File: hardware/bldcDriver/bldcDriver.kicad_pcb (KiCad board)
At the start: 2 copper layers, 5 parts, among them Q1 NMOS, U2 STM32G431RBTx

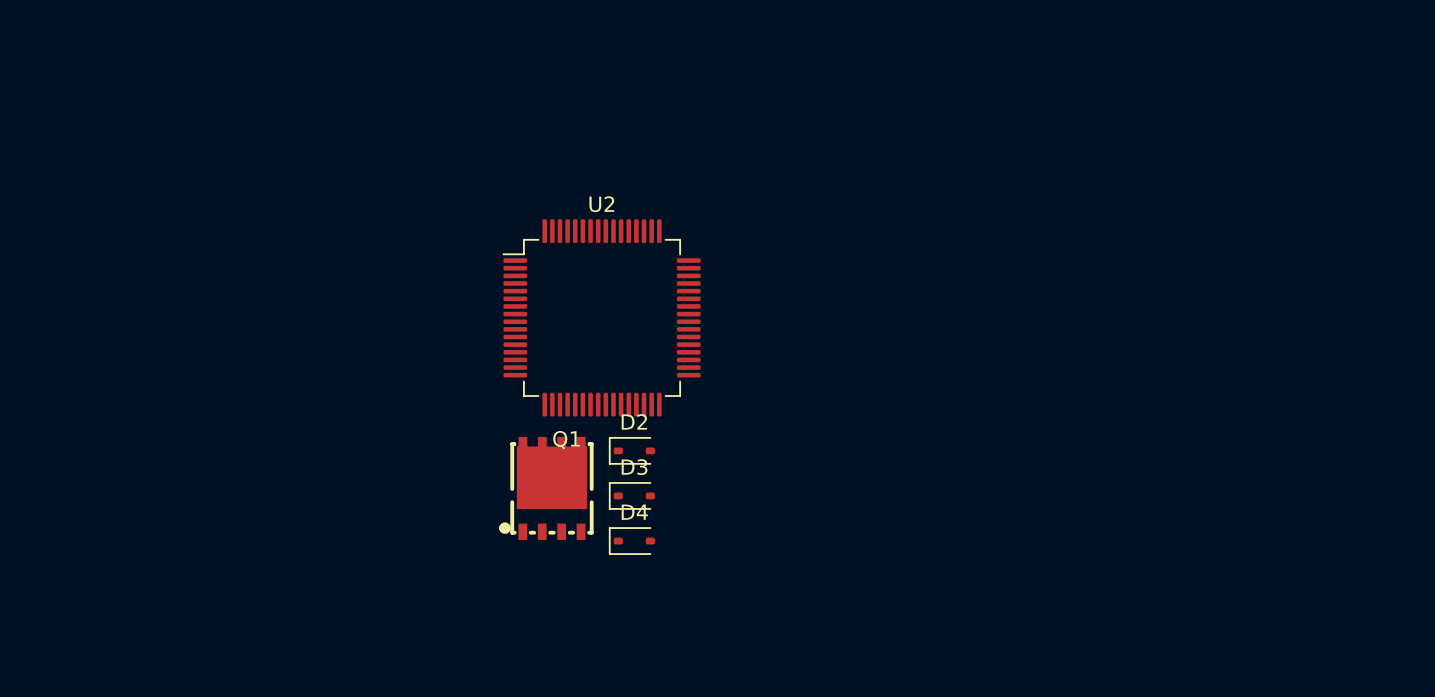
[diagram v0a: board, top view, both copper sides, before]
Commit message: motorDriver sch update
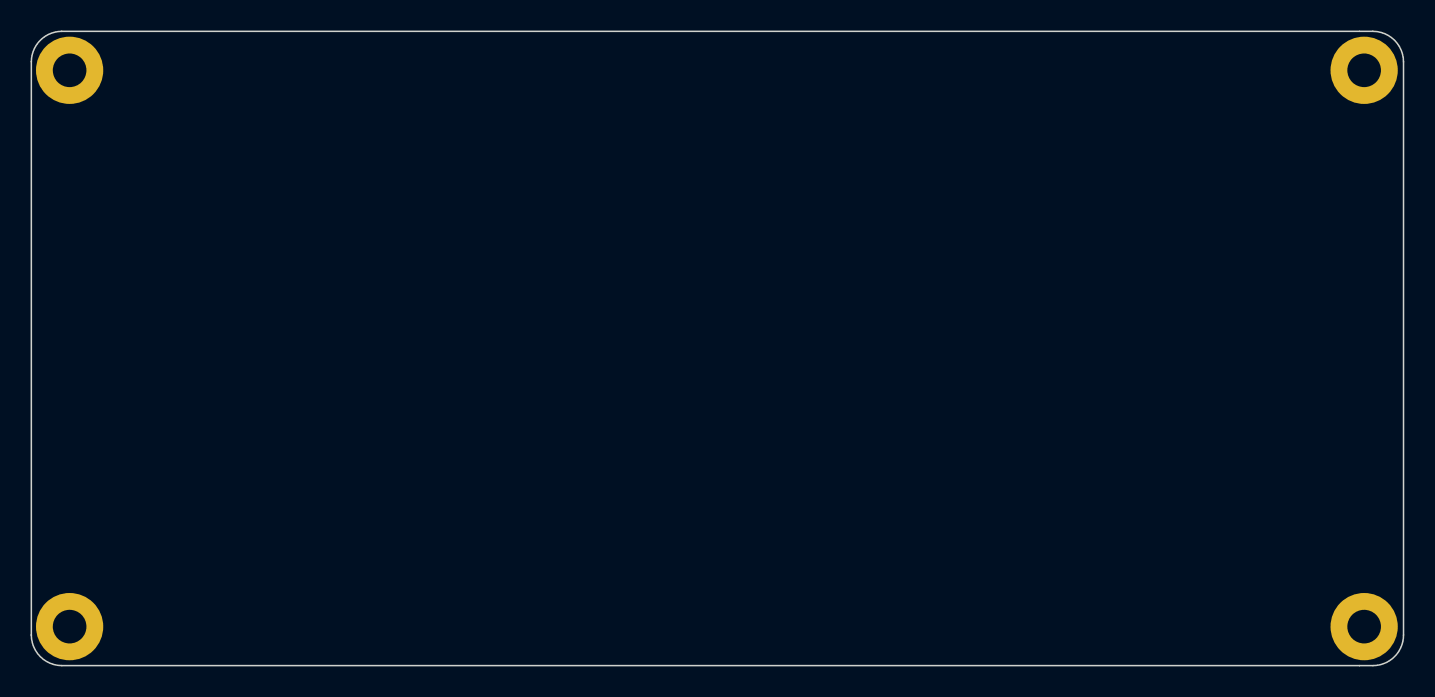
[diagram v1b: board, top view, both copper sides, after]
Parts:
- removed D2, D3, D4: 1N5819WS, Diode_SMD:D_SOD-323
- removed Q1: NMOS, balancerDriver:PDFN-8_L4.9-W5.8-P1.27-LS6.1-BL
- removed U2: STM32G431RBTx, Package_QFP:LQFP-64_10x10mm_P0.5mm
- added ?: , , F.Cu at (56.0, 57.6)
- added ?: , , F.Cu at (140.7, 57.6)
- added ?: , , F.Cu at (140.7, 94.0)
- added ?: , , F.Cu at (56.0, 94.0)
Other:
- board outline added: 89.8 x 41.5 mm

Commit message: update driver pcb
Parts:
- added C1: 10n, Capacitor_SMD:C_0603_1608Metric_Pad1.08x0.95mm_HandSolder, B.Cu at (46.1, 39.1)
- added C10: 47u, Capacitor_SMD:C_1206_3216Metric_Pad1.33x1.80mm_HandSolder, B.Cu at (71.5, 43.2)
- added C11: 10u, Capacitor_SMD:C_0805_2012Metric_Pad1.18x1.45mm_HandSolder, F.Cu at (45.0, 33.7)
- added C12: 100nF/25V, Capacitor_SMD:C_0603_1608Metric_Pad1.08x0.95mm_HandSolder, B.Cu at (96.2, 40.3)
- added C14: 100n, Capacitor_SMD:C_0603_1608Metric_Pad1.08x0.95mm_HandSolder, B.Cu at (103.3, 46.0)
- added C15: 100n, Capacitor_SMD:C_0603_1608Metric_Pad1.08x0.95mm_HandSolder, B.Cu at (106.8, 42.8)
- added C16: 100n, Capacitor_SMD:C_0603_1608Metric_Pad1.08x0.95mm_HandSolder, B.Cu at (106.8, 39.4)
- added C17: 100n, Capacitor_SMD:C_0603_1608Metric_Pad1.08x0.95mm_HandSolder, F.Cu at (89.8, 53.2)
- added C18: 100n, Capacitor_SMD:C_0603_1608Metric_Pad1.08x0.95mm_HandSolder, F.Cu at (74.8, 40.6)
- added C19: 100n, Capacitor_SMD:C_0603_1608Metric_Pad1.08x0.95mm_HandSolder, F.Cu at (90.0, 40.6)
- added C2: 47u, Capacitor_SMD:C_1206_3216Metric_Pad1.33x1.80mm_HandSolder, B.Cu at (56.4, 35.8)
- added C20: 100n, Capacitor_SMD:C_0603_1608Metric_Pad1.08x0.95mm_HandSolder, F.Cu at (74.3, 51.0)
- added C21: 470n, Capacitor_SMD:C_0603_1608Metric_Pad1.08x0.95mm_HandSolder, F.Cu at (85.4, 55.2)
- added C25: 100nF/25V, Capacitor_SMD:C_0603_1608Metric_Pad1.08x0.95mm_HandSolder, B.Cu at (67.6, 47.9)
- added C26: 100n, Capacitor_SMD:C_0603_1608Metric_Pad1.08x0.95mm_HandSolder, B.Cu at (60.3, 41.7)
- added C27: 100n, Capacitor_SMD:C_0603_1608Metric_Pad1.08x0.95mm_HandSolder, B.Cu at (57.3, 45.5)
- added C28: 100n, Capacitor_SMD:C_0603_1608Metric_Pad1.08x0.95mm_HandSolder, B.Cu at (57.3, 48.8)
- added C29: 22uF/25V, Capacitor_SMD:C_0805_2012Metric_Pad1.18x1.45mm_HandSolder, B.Cu at (40.8, 52.5)
- added C3: 47u, Capacitor_SMD:C_1206_3216Metric_Pad1.33x1.80mm_HandSolder, B.Cu at (54.3, 35.8)
- added C30: 1n, Capacitor_SMD:C_0603_1608Metric_Pad1.08x0.95mm_HandSolder, B.Cu at (61.5, 50.6)
- added C31: 22uF/25V, Capacitor_SMD:C_0805_2012Metric_Pad1.18x1.45mm_HandSolder, B.Cu at (119.3, 52.4)
- added C32: 1n, Capacitor_SMD:C_0603_1608Metric_Pad1.08x0.95mm_HandSolder, B.Cu at (97.6, 50.0)
- added C33: 22uF/25V, Capacitor_SMD:C_0805_2012Metric_Pad1.18x1.45mm_HandSolder, B.Cu at (40.9, 56.9)
- added C34: 22uF/25V, Capacitor_SMD:C_0805_2012Metric_Pad1.18x1.45mm_HandSolder, B.Cu at (119.3, 54.9)
- added C35: 22uF/25V, Capacitor_SMD:C_0805_2012Metric_Pad1.18x1.45mm_HandSolder, B.Cu at (39.4, 66.4)
- added C36: 1n, Capacitor_SMD:C_0603_1608Metric_Pad1.08x0.95mm_HandSolder, B.Cu at (63.1, 62.1)
- added C37: 22uF/25V, Capacitor_SMD:C_0805_2012Metric_Pad1.18x1.45mm_HandSolder, B.Cu at (119.3, 66.0)
- added C38: 1n, Capacitor_SMD:C_0603_1608Metric_Pad1.08x0.95mm_HandSolder, B.Cu at (97.8, 70.4)
- added C39: 22uF/25V, Capacitor_SMD:C_0805_2012Metric_Pad1.18x1.45mm_HandSolder, B.Cu at (39.4, 68.6)
- added C4: 47u, Capacitor_SMD:C_1206_3216Metric_Pad1.33x1.80mm_HandSolder, B.Cu at (51.9, 35.8)
- added C40: 22uF/25V, Capacitor_SMD:C_0805_2012Metric_Pad1.18x1.45mm_HandSolder, B.Cu at (119.3, 63.7)
- added C41: 22uF/25V, Capacitor_SMD:C_0805_2012Metric_Pad1.18x1.45mm_HandSolder, B.Cu at (39.5, 61.6)
- added C42: 10u, Capacitor_SMD:C_0805_2012Metric_Pad1.18x1.45mm_HandSolder, F.Cu at (49.9, 41.2)
- added C43: 22uF/25V, Capacitor_SMD:C_0805_2012Metric_Pad1.18x1.45mm_HandSolder, B.Cu at (119.2, 58.0)
- added C44: 100n, Capacitor_SMD:C_0603_1608Metric_Pad1.08x0.95mm_HandSolder, F.Cu at (49.7, 39.3)
- added C45: 22uF/25V, Capacitor_SMD:C_0805_2012Metric_Pad1.18x1.45mm_HandSolder, B.Cu at (39.5, 63.9)
- added C46: 22uF/25V, Capacitor_SMD:C_0805_2012Metric_Pad1.18x1.45mm_HandSolder, B.Cu at (119.2, 60.3)
- added C47: 10n, Capacitor_SMD:C_0603_1608Metric_Pad1.08x0.95mm_HandSolder, F.Cu at (84.2, 69.2)
- added C48: 100n, Capacitor_SMD:C_0603_1608Metric_Pad1.08x0.95mm_HandSolder, F.Cu at (84.2, 67.7)
- added C49: 2.2U, Capacitor_SMD:C_0603_1608Metric_Pad1.08x0.95mm_HandSolder, F.Cu at (80.7, 63.8)
- added C5: 22u, Capacitor_SMD:C_0805_2012Metric_Pad1.18x1.45mm_HandSolder, B.Cu at (39.0, 43.9)
- added C50: 100n, Capacitor_SMD:C_0603_1608Metric_Pad1.08x0.95mm_HandSolder, F.Cu at (84.2, 66.2)
- added C51: 100n, Capacitor_SMD:C_0603_1608Metric_Pad1.08x0.95mm_HandSolder, F.Cu at (47.0, 33.4)
- added C52: 4.7u, Capacitor_SMD:C_0603_1608Metric_Pad1.08x0.95mm_HandSolder, F.Cu at (110.3, 36.2)
- added C53: 100n, Capacitor_SMD:C_0603_1608Metric_Pad1.08x0.95mm_HandSolder, F.Cu at (110.3, 37.7)
- added C54: 4.7u, Capacitor_SMD:C_0603_1608Metric_Pad1.08x0.95mm_HandSolder, F.Cu at (110.2, 42.4)
- added C55: 100n, Capacitor_SMD:C_0603_1608Metric_Pad1.08x0.95mm_HandSolder, F.Cu at (110.2, 43.9)
- added C56: 4.7u, Capacitor_SMD:C_0603_1608Metric_Pad1.08x0.95mm_HandSolder, F.Cu at (143.0, 51.9)
- added C57: 100n, Capacitor_SMD:C_0603_1608Metric_Pad1.08x0.95mm_HandSolder, F.Cu at (143.0, 53.4)
- added C58: 100n, Capacitor_SMD:C_0603_1608Metric_Pad1.08x0.95mm_HandSolder, F.Cu at (139.8, 45.2)
- added C59: 4.7u, Capacitor_SMD:C_0603_1608Metric_Pad1.08x0.95mm_HandSolder, F.Cu at (142.8, 41.6)
- added C6: 22u, Capacitor_SMD:C_0805_2012Metric_Pad1.18x1.45mm_HandSolder, B.Cu at (41.1, 43.9)
- added C60: 100n, Capacitor_SMD:C_0603_1608Metric_Pad1.08x0.95mm_HandSolder, F.Cu at (142.8, 40.1)
- added C61: 100n, Capacitor_SMD:C_0603_1608Metric_Pad1.08x0.95mm_HandSolder, F.Cu at (148.2, 64.1)
- added C62: 2.2n, Capacitor_SMD:C_0603_1608Metric_Pad1.08x0.95mm_HandSolder, F.Cu at (146.2, 62.5)
- added C63: 2.2n, Capacitor_SMD:C_0603_1608Metric_Pad1.08x0.95mm_HandSolder, F.Cu at (151.9, 63.5)
- added C64: 2.2n, Capacitor_SMD:C_0603_1608Metric_Pad1.08x0.95mm_HandSolder, F.Cu at (143.3, 28.0)
- added C65: 2.2n, Capacitor_SMD:C_0603_1608Metric_Pad1.08x0.95mm_HandSolder, F.Cu at (143.2, 26.4)
- added C66: 100n, Capacitor_SMD:C_0603_1608Metric_Pad1.08x0.95mm_HandSolder, F.Cu at (146.5, 27.7)
- added C67: 12p, Capacitor_SMD:C_0603_1608Metric_Pad1.08x0.95mm_HandSolder, F.Cu at (71.2, 40.6)
- added C68: 12p, Capacitor_SMD:C_0603_1608Metric_Pad1.08x0.95mm_HandSolder, F.Cu at (71.3, 48.8)
- added C7: 100n, Capacitor_SMD:C_0603_1608Metric_Pad1.08x0.95mm_HandSolder, B.Cu at (40.1, 41.1)
- added C8: 100n, Capacitor_SMD:C_0603_1608Metric_Pad1.08x0.95mm_HandSolder, B.Cu at (58.5, 35.1)
- added C9: 47u, Capacitor_SMD:C_1206_3216Metric_Pad1.33x1.80mm_HandSolder, B.Cu at (67.4, 39.5)
- added CN1: MR30PW-F, balancerDriver:CONN-TH_MR30PW-F, F.Cu at (69.1, 61.8)
- added CN2: MR30PW-F, balancerDriver:CONN-TH_MR30PW-F, F.Cu at (91.7, 60.3)
- added D1: LED, LED_SMD:LED_0603_1608Metric_Pad1.05x0.95mm_HandSolder, B.Cu at (54.1, 32.1)
- added D10: 1N5819WS, Diode_SMD:D_SOD-323, B.Cu at (60.2, 39.9)
- added D11: 1N5819WS, Diode_SMD:D_SOD-323, B.Cu at (55.5, 45.5)
- added D12: 1N5819WS, Diode_SMD:D_SOD-323, B.Cu at (55.5, 48.8)
- added D2: 1N5819WS, Diode_SMD:D_SOD-323, B.Cu at (107.5, 45.8)
- added D3: 1N5819WS, Diode_SMD:D_SOD-323, B.Cu at (108.6, 42.7)
- added D4: 1N5819WS, Diode_SMD:D_SOD-323, B.Cu at (108.6, 39.4)
- added D8: 1N5712UR, Diode_SMD:D_MELF, B.Cu at (39.9, 34.9)
- added D9: 1N5712UR, Diode_SMD:D_MELF, B.Cu at (76.7, 36.9)
- added FB2: FerriteBead, Capacitor_SMD:C_1206_3216Metric_Pad1.33x1.80mm_HandSolder, B.Cu at (54.6, 40.4)
- added FB3: FerriteBead, Capacitor_SMD:C_0603_1608Metric_Pad1.08x0.95mm_HandSolder, F.Cu at (110.3, 34.7)
- added J1: Conn_01x02, balancerDriver:CONN-TH_XT30UPB-M, F.Cu at (36.0, 52.9)
- added J2: Conn_01x06, Connector_PinSocket_2.54mm:PinSocket_1x06_P2.54mm_Vertical, F.Cu at (93.4, 33.1)
- added J3: Conn_01x06, balancerDriver:CONN-SMD_BM06B-GHS-TBT-LF-SN, F.Cu at (117.8, 42.7)
- added J4: Conn_01x03, balancerDriver:CONN-SMD_3P-P1.00_WAFER-SH1.0-3PWB, F.Cu at (99.7, 34.3)
- added J5: Conn_01x06, balancerDriver:CONN-SMD_BM06B-GHS-TBT-LF-SN, F.Cu at (39.6, 41.5)
- added L1: 10u, Inductor_SMD:L_Sumida_CDMC6D28_7.25x6.5mm, B.Cu at (46.2, 34.5)
- added L2: 10u, Inductor_SMD:L_Taiyo-Yuden_MD-4040, B.Cu at (70.9, 33.1)
- added Q1: KNY3406C, balancerDriver:PDFN-8_L4.9-W5.8-P1.27-LS6.1-BL, B.Cu at (45.5, 56.0)
- added Q10: KNY3406C, balancerDriver:PDFN-8_L4.9-W5.8-P1.27-LS6.1-BL, B.Cu at (53.7, 62.0)
- added Q11: KNY3406C, balancerDriver:PDFN-8_L4.9-W5.8-P1.27-LS6.1-BL, B.Cu at (113.4, 59.2)
- added Q12: KNY3406C, balancerDriver:PDFN-8_L4.9-W5.8-P1.27-LS6.1-BL, B.Cu at (105.7, 59.2)
- added Q13: PMOS, Package_TO_SOT_SMD:SOT-23, B.Cu at (61.2, 35.1)
- added Q14: S8050, Package_TO_SOT_SMD:SOT-23, B.Cu at (65.0, 32.8)
- added Q2: KNY3406C, balancerDriver:PDFN-8_L4.9-W5.8-P1.27-LS6.1-BL, B.Cu at (53.3, 56.2)
- added Q3: KNY3406C, balancerDriver:PDFN-8_L4.9-W5.8-P1.27-LS6.1-BL, B.Cu at (113.2, 53.6)
- added Q4: KNY3406C, balancerDriver:PDFN-8_L4.9-W5.8-P1.27-LS6.1-BL, B.Cu at (105.7, 53.7)
- added Q5: KNY3406C, balancerDriver:PDFN-8_L4.9-W5.8-P1.27-LS6.1-BL, B.Cu at (45.7, 67.5)
- added Q6: KNY3406C, balancerDriver:PDFN-8_L4.9-W5.8-P1.27-LS6.1-BL, B.Cu at (53.5, 67.5)
- added Q7: KNY3406C, balancerDriver:PDFN-8_L4.9-W5.8-P1.27-LS6.1-BL, B.Cu at (113.3, 64.7)
- added Q8: KNY3406C, balancerDriver:PDFN-8_L4.9-W5.8-P1.27-LS6.1-BL, B.Cu at (105.8, 64.7)
- added Q9: KNY3406C, balancerDriver:PDFN-8_L4.9-W5.8-P1.27-LS6.1-BL, B.Cu at (45.6, 61.9)
- added R1: 10k, Resistor_SMD:R_0603_1608Metric_Pad0.98x0.95mm_HandSolder, B.Cu at (51.1, 40.4)
- added R10: 100R, Resistor_SMD:R_0603_1608Metric_Pad0.98x0.95mm_HandSolder, B.Cu at (95.7, 51.6)
- added R11: 20mR, Resistor_SMD:R_2512_6332Metric_Pad1.40x3.35mm_HandSolder, B.Cu at (61.7, 55.4)
- added R12: 20mR, Resistor_SMD:R_2512_6332Metric_Pad1.40x3.35mm_HandSolder, B.Cu at (97.8, 54.5)
- added R13: 10k, Resistor_SMD:R_0603_1608Metric_Pad0.98x0.95mm_HandSolder, B.Cu at (49.4, 52.5)
- added R14: 10k, Resistor_SMD:R_0603_1608Metric_Pad0.98x0.95mm_HandSolder, B.Cu at (59.3, 58.3)
- added R15: 10k, Resistor_SMD:R_0603_1608Metric_Pad0.98x0.95mm_HandSolder, B.Cu at (112.6, 50.1)
- added R16: 10k, Resistor_SMD:R_0603_1608Metric_Pad0.98x0.95mm_HandSolder, B.Cu at (105.5, 50.1)
- added R17: 10R, Resistor_SMD:R_0603_1608Metric_Pad0.98x0.95mm_HandSolder, B.Cu at (49.4, 50.9)
- added R18: 10R, Resistor_SMD:R_0603_1608Metric_Pad0.98x0.95mm_HandSolder, B.Cu at (63.1, 58.3)
- added R19: 10R, Resistor_SMD:R_0603_1608Metric_Pad0.98x0.95mm_HandSolder, B.Cu at (109.1, 50.1)
- added R2: 3.3k, Resistor_SMD:R_0603_1608Metric_Pad0.98x0.95mm_HandSolder, B.Cu at (51.1, 44.0)
- added R20: 10R, Resistor_SMD:R_0603_1608Metric_Pad0.98x0.95mm_HandSolder, B.Cu at (101.7, 50.0)
- added R21: 100R, Resistor_SMD:R_0603_1608Metric_Pad0.98x0.95mm_HandSolder, B.Cu at (59.6, 63.8)
- added R22: 100R, Resistor_SMD:R_0603_1608Metric_Pad0.98x0.95mm_HandSolder, B.Cu at (63.6, 63.8)
- added R23: 100R, Resistor_SMD:R_0603_1608Metric_Pad0.98x0.95mm_HandSolder, B.Cu at (99.6, 68.6)
- added R24: 100R, Resistor_SMD:R_0603_1608Metric_Pad0.98x0.95mm_HandSolder, B.Cu at (95.7, 68.6)
- added R25: 20mR, Resistor_SMD:R_2512_6332Metric_Pad1.40x3.35mm_HandSolder, B.Cu at (61.6, 66.7)
- added R26: 20mR, Resistor_SMD:R_2512_6332Metric_Pad1.40x3.35mm_HandSolder, B.Cu at (97.7, 65.6)
- added R27: 10k, Resistor_SMD:R_0603_1608Metric_Pad0.98x0.95mm_HandSolder, B.Cu at (49.6, 70.9)
- added R28: 10k, Resistor_SMD:R_0603_1608Metric_Pad0.98x0.95mm_HandSolder, B.Cu at (59.3, 69.6)
- added R29: 10k, Resistor_SMD:R_0603_1608Metric_Pad0.98x0.95mm_HandSolder, B.Cu at (110.4, 68.3)
- added R3: 4.7k, Resistor_SMD:R_0603_1608Metric_Pad0.98x0.95mm_HandSolder, B.Cu at (57.6, 32.1)
- added R30: 10k, Resistor_SMD:R_0603_1608Metric_Pad0.98x0.95mm_HandSolder, B.Cu at (104.1, 68.7)
- added R31: 10R, Resistor_SMD:R_0603_1608Metric_Pad0.98x0.95mm_HandSolder, B.Cu at (53.3, 70.9)
- added R32: 10R, Resistor_SMD:R_0603_1608Metric_Pad0.98x0.95mm_HandSolder, B.Cu at (63.2, 69.6)
- added R33: 10R, Resistor_SMD:R_0603_1608Metric_Pad0.98x0.95mm_HandSolder, B.Cu at (110.4, 70.0)
- added R34: 10R, Resistor_SMD:R_0603_1608Metric_Pad0.98x0.95mm_HandSolder, B.Cu at (104.2, 70.5)
- added R35: 1k, Resistor_SMD:R_0603_1608Metric_Pad0.98x0.95mm_HandSolder, F.Cu at (110.2, 39.2)
- added R36: 1k, Resistor_SMD:R_0603_1608Metric_Pad0.98x0.95mm_HandSolder, F.Cu at (110.2, 40.8)
- added R37: 10k, Resistor_SMD:R_0603_1608Metric_Pad0.98x0.95mm_HandSolder, B.Cu at (64.9, 35.7)
- added R38: 10k, Resistor_SMD:R_0603_1608Metric_Pad0.98x0.95mm_HandSolder, B.Cu at (65.3, 38.6)
- added R39: 63.4k, Resistor_SMD:R_0603_1608Metric_Pad0.98x0.95mm_HandSolder, B.Cu at (70.8, 41.3)
- added R4: 10k, Resistor_SMD:R_0603_1608Metric_Pad0.98x0.95mm_HandSolder, B.Cu at (60.0, 37.9)
- added R40: 3.3k, Resistor_SMD:R_0603_1608Metric_Pad0.98x0.95mm_HandSolder, B.Cu at (70.8, 39.8)
- added R41: 10k, Resistor_SMD:R_0603_1608Metric_Pad0.98x0.95mm_HandSolder, B.Cu at (58.6, 61.1)
- added R42: 10k, Resistor_SMD:R_0603_1608Metric_Pad0.98x0.95mm_HandSolder, B.Cu at (65.9, 59.3)
- added R43: 10k, Resistor_SMD:R_0603_1608Metric_Pad0.98x0.95mm_HandSolder, B.Cu at (99.5, 61.8)
- added R44: 10k, Resistor_SMD:R_0603_1608Metric_Pad0.98x0.95mm_HandSolder, B.Cu at (99.6, 57.9)
- added R45: 10R, Resistor_SMD:R_0603_1608Metric_Pad0.98x0.95mm_HandSolder, B.Cu at (60.3, 61.1)
- added R46: 10R, Resistor_SMD:R_0603_1608Metric_Pad0.98x0.95mm_HandSolder, B.Cu at (63.1, 60.3)
- added R47: 10R, Resistor_SMD:R_0603_1608Metric_Pad0.98x0.95mm_HandSolder, B.Cu at (95.8, 61.8)
- added R48: 10R, Resistor_SMD:R_0603_1608Metric_Pad0.98x0.95mm_HandSolder, B.Cu at (95.7, 57.8)
- added R49: 10K, Resistor_SMD:R_0603_1608Metric_Pad0.98x0.95mm_HandSolder, F.Cu at (84.2, 64.4)
- added R5: 100R, Resistor_SMD:R_0603_1608Metric_Pad0.98x0.95mm_HandSolder, B.Cu at (61.2, 32.2)
- added R50: 1k, Resistor_SMD:R_0603_1608Metric_Pad0.98x0.95mm_HandSolder, F.Cu at (110.2, 45.4)
- added R51: 1k, Resistor_SMD:R_0603_1608Metric_Pad0.98x0.95mm_HandSolder, F.Cu at (110.2, 46.9)
- added R52: 10k, Resistor_SMD:R_0603_1608Metric_Pad0.98x0.95mm_HandSolder, F.Cu at (139.9, 69.9)
- added R53: 1k, Resistor_SMD:R_0603_1608Metric_Pad0.98x0.95mm_HandSolder, F.Cu at (139.9, 68.3)
- added R54: 10k, Resistor_SMD:R_0603_1608Metric_Pad0.98x0.95mm_HandSolder, F.Cu at (139.9, 65.0)
- added R55: 100R, Resistor_SMD:R_0603_1608Metric_Pad0.98x0.95mm_HandSolder, F.Cu at (144.1, 64.1)
- added R56: 1k, Resistor_SMD:R_0603_1608Metric_Pad0.98x0.95mm_HandSolder, F.Cu at (139.9, 66.7)
- added R57: 1k, Resistor_SMD:R_0603_1608Metric_Pad0.98x0.95mm_HandSolder, F.Cu at (151.8, 70.3)
- added R58: 10k, Resistor_SMD:R_0603_1608Metric_Pad0.98x0.95mm_HandSolder, F.Cu at (148.2, 71.5)
- added R59: 1k, Resistor_SMD:R_0603_1608Metric_Pad0.98x0.95mm_HandSolder, F.Cu at (152.7, 67.7)
- added R6: 1k, Resistor_SMD:R_0603_1608Metric_Pad0.98x0.95mm_HandSolder, B.Cu at (67.7, 32.8)
- added R60: 10k, Resistor_SMD:R_0603_1608Metric_Pad0.98x0.95mm_HandSolder, F.Cu at (151.0, 67.7)
- added R61: 100R, Resistor_SMD:R_0603_1608Metric_Pad0.98x0.95mm_HandSolder, F.Cu at (151.9, 65.1)
- added R62: 1k, Resistor_SMD:R_0603_1608Metric_Pad0.98x0.95mm_HandSolder, F.Cu at (135.6, 30.2)
- added R63: 1k, Resistor_SMD:R_0603_1608Metric_Pad0.98x0.95mm_HandSolder, F.Cu at (136.3, 32.6)
- added R64: 10k, Resistor_SMD:R_0603_1608Metric_Pad0.98x0.95mm_HandSolder, F.Cu at (136.3, 34.2)
- added R65: 10k, Resistor_SMD:R_0603_1608Metric_Pad0.98x0.95mm_HandSolder, F.Cu at (137.2, 30.1)
- added R66: 100R, Resistor_SMD:R_0603_1608Metric_Pad0.98x0.95mm_HandSolder, F.Cu at (139.8, 28.0)
- added R67: 1k, Resistor_SMD:R_0603_1608Metric_Pad0.98x0.95mm_HandSolder, F.Cu at (148.2, 33.4)
- added R68: 1k, Resistor_SMD:R_0603_1608Metric_Pad0.98x0.95mm_HandSolder, F.Cu at (146.5, 34.7)
- added R69: 10k, Resistor_SMD:R_0603_1608Metric_Pad0.98x0.95mm_HandSolder, F.Cu at (143.9, 35.4)
- added R7: 100R, Resistor_SMD:R_0603_1608Metric_Pad0.98x0.95mm_HandSolder, B.Cu at (59.6, 52.5)
- added R70: 10k, Resistor_SMD:R_0603_1608Metric_Pad0.98x0.95mm_HandSolder, F.Cu at (146.5, 31.2)
- added R71: 100R, Resistor_SMD:R_0603_1608Metric_Pad0.98x0.95mm_HandSolder, F.Cu at (148.3, 29.4)
- added R72: 4.7k, Resistor_SMD:R_0603_1608Metric_Pad0.98x0.95mm_HandSolder, F.Cu at (75.4, 70.3)
- added R73: 4.7k, Resistor_SMD:R_0603_1608Metric_Pad0.98x0.95mm_HandSolder, F.Cu at (75.4, 68.8)
- added R74: 4.7k, Resistor_SMD:R_0603_1608Metric_Pad0.98x0.95mm_HandSolder, F.Cu at (75.4, 67.3)
- added R8: 100R, Resistor_SMD:R_0603_1608Metric_Pad0.98x0.95mm_HandSolder, B.Cu at (63.7, 52.5)
- added R9: 100R, Resistor_SMD:R_0603_1608Metric_Pad0.98x0.95mm_HandSolder, B.Cu at (99.7, 51.6)
- added U1: FD6288T, balancerDriver:TSSOP-20_L6.5-W4.4-P0.65-LS6.4-BL, B.Cu at (101.4, 41.7)
- added U10: AMS1117, Package_TO_SOT_SMD:SOT-223-3_TabPin2, F.Cu at (52.5, 34.7)
- added U11: FD6288T, balancerDriver:TSSOP-20_L6.5-W4.4-P0.65-LS6.4-BL, B.Cu at (62.4, 45.8)
- added U2: STM32G431RBTx, Package_QFP:LQFP-64_10x10mm_P0.5mm, F.Cu at (82.5, 46.7)
- added U3: TPS5430DDA, Package_SO:TI_SO-PowerPAD-8_ThermalVias, B.Cu at (45.8, 42.9)
- added U5: MPU6500, balancerDriver:QFN-24_L3.0-W3.0-P0.40-BL-EP, F.Cu at (79.7, 68.0)
- added U6: TLV9062xD, Package_SO:SOIC-8_3.9x4.9mm_P1.27mm, F.Cu at (143.5, 47.1)
- added U7: MT3608, Package_TO_SOT_SMD:SOT-23-6, B.Cu at (70.8, 37.2)
- added U8: TLV9062xD, Package_SO:SOIC-8_3.9x4.9mm_P1.27mm, F.Cu at (146.2, 67.8)
- added U9: TLV9062xD, Package_SO:SOIC-8_3.9x4.9mm_P1.27mm, F.Cu at (141.9, 31.7)
- added Y1: 25MHz, Crystal:Crystal_SMD_SeikoEpson_FA238-4Pin_3.2x2.5mm_HandSoldering, F.Cu at (71.3, 44.6)
- moved ? 32.2 mm to (35.0, 33.2)
- moved ? 32.2 mm to (35.0, 69.6)
- moved ? 32.2 mm to (119.7, 33.2)
- moved ? 32.2 mm to (119.7, 69.6)
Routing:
- net /inverter/1SH_U: track 0.00 -> 35.7 mm, vias 0 -> 2
- net /inverter/1GH_B: track 0.00 -> 31.8 mm, vias 0 -> 2
- net Net-(Q9-G): track 0.00 -> 24.0 mm
- net /inverter/1GL_B: track 0.00 -> 22.1 mm, vias 0 -> 2
- net +3V3: track 0.00 -> 20.8 mm
- net /inverter/1GH_C: track 0.00 -> 16.8 mm, vias 0 -> 2
- net /TIM1_CH1: track 0.00 -> 16.5 mm, vias 0 -> 1
- net /inverter/1GL_C: track 0.00 -> 14.2 mm
- net /inverter/1GH_A: track 0.00 -> 13.6 mm
- net /TIM1_CH3: track 0.00 -> 13.2 mm, vias 0 -> 1
- net /TIM1_CH2: track 0.00 -> 13.1 mm, vias 0 -> 1
- net Net-(Q10-G): track 0.00 -> 12.4 mm
- net /inverter/1GL_A: track 0.00 -> 11.6 mm, vias 0 -> 2
- net /YI: track 0.00 -> 10.2 mm
- net /inverter/1SH_V: track 0.00 -> 9.31 mm
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- added copper zone on F.Cu, net +3V3
- added copper zone on B.Cu, net +5V
- added copper zone on B.Cu, net +BATT
- added copper zone on B.Cu, net /inverter/1SH_U
- added copper zone on B.Cu, net /inverter/1SH_V
- added copper zone on B.Cu, net /inverter/1SH_W
- added copper zone on B.Cu, net GNDD
- added copper zone on In2.Cu, net GNDPWR
- added copper zone on B.Cu, net Net-(D8-K)
- added copper zone on B.Cu, net Net-(Q2-S-Pad1)
- added copper zone on B.Cu, net Net-(Q6-S-Pad1)
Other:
- copper layers 2 -> 4

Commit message: update pcbs
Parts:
- moved R57 109.4 mm to (42.4, 67.7), turned to -90 degrees
- moved R59 107.7 mm to (45.0, 68.6), turned to 0 degrees
- moved R58 107.2 mm to (41.2, 64.1), turned to 90 degrees
- moved R60 106.0 mm to (45.0, 66.9), turned to 0 degrees
- moved R61 104.3 mm to (47.6, 67.8), turned to -90 degrees
- moved C63 102.7 mm to (49.2, 67.8), turned to -90 degrees
- moved U8 101.4 mm to (44.9, 62.1), turned to -90 degrees
- moved C61 99.6 mm to (48.6, 64.1), turned to -90 degrees
- moved R52 98.1 mm to (42.8, 55.9), turned to 90 degrees
- moved R53 96.3 mm to (44.4, 55.8), turned to 90 degrees
- moved C62 96.0 mm to (50.2, 62.1), turned to 90 degrees
- moved R55 95.6 mm to (48.6, 60.0), turned to -90 degrees
- moved R56 94.5 mm to (46.0, 55.8), turned to 90 degrees
- moved R54 92.6 mm to (47.7, 55.8), turned to -90 degrees
- moved C57 70.0 mm to (74.0, 64.8), turned to 90 degrees
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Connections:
- C30 pad 1: /1A_iSENSOR_N -> /1A_ISENSOR_N
- C32 pad 1: /2A_iSENSOR_N -> /2A_ISENSOR_N
- C32 pad 2: /2A_iSENSOR_P -> /2A_ISENSOR_P
- C36 pad 1: /1B_iSENSOR_N -> /1B_ISENSOR_N
- C36 pad 2: /1B_iSENSOR_P -> /1B_ISENSOR_P
- C38 pad 1: /2B_iSENSOR_N -> /2B_ISENSOR_N
- C38 pad 2: /2B_iSENSOR_P -> /2B_ISENSOR_P
- CN2 pad 1: /inverter/2SH_U -> /inverter/2SH_W
- CN2 pad 3: /inverter/2SH_W -> /inverter/2SH_U
- R10 pad 2: /2A_iSENSOR_N -> /2A_ISENSOR_N
- R21 pad 2: /1B_iSENSOR_P -> /1B_ISENSOR_P
- R22 pad 2: /1B_iSENSOR_N -> /1B_ISENSOR_N
- R23 pad 2: /2B_iSENSOR_P -> /2B_ISENSOR_P
- R24 pad 2: /2B_iSENSOR_N -> /2B_ISENSOR_N
- R8 pad 2: /1A_iSENSOR_N -> /1A_ISENSOR_N
- R9 pad 2: /2A_iSENSOR_P -> /2A_ISENSOR_P
- U2 pad 21: /TIM8_CH1N -> /TIM1_CH1N
- U2 pad 35: /TIM1_CH1N -> unconnected-(U2-PB13-Pad35)
- U2 pad 56: unconnected-(U2-PB3-Pad56) -> /TIM8_CH1N
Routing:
- net /inverter/2GH_B: track 0.00 -> 29.5 mm, vias 0 -> 2
- net /inverter/2SH_V: track 0.00 -> 28.0 mm, vias 0 -> 9
- net /inverter/2GL_B: track 0.00 -> 27.8 mm, vias 0 -> 2
- net /inverter/2GH_C: track 0.00 -> 26.4 mm, vias 0 -> 2
- net /inverter/2SH_U: track 0.00 -> 24.7 mm, vias 0 -> 9
- net +3V3: track 20.8 -> 44.5 mm, vias 0 -> 1
- net /inverter/2GL_C: track 0.00 -> 22.2 mm, vias 0 -> 2
- net /TIM1_CH3N: track 0.00 -> 22.1 mm, vias 0 -> 3
- net /inverter/2SH_W: track 0.00 -> 20.5 mm, vias 0 -> 9
- net /TIM1_CH2N: track 0.00 -> 20.4 mm, vias 0 -> 1
- net /inverter/1SH_W: track 4.72 -> 21.7 mm, vias 0 -> 9
- net /inverter/1SH_V: track 9.31 -> 26.1 mm, vias 0 -> 9
- net Net-(Q11-G): track 0.00 -> 16.6 mm
- net /TIM8_CH3N: track 0.00 -> 14.9 mm, vias 0 -> 1
- net /TIM8_CH1N: track 0.00 -> 14.9 mm, vias 0 -> 1
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- added copper zone on B.Cu, net /inverter/2SH_U
- added copper zone on B.Cu, net /inverter/2SH_V
- added copper zone on B.Cu, net /inverter/2SH_W
- added copper zone on B.Cu, net Net-(Q4-S-Pad1)
- added copper zone on B.Cu, net Net-(Q8-S-Pad1)

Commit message: update pcbs
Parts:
- moved C49 1.66 mm to (77.7, 59.7), turned to 180 degrees
- moved C17 1.37 mm to (88.4, 53.1)
- moved R72 1.21 mm to (81.8, 55.8)
- moved R73 1.21 mm to (81.8, 57.3)
- moved R74 1.21 mm to (81.9, 58.8)
- moved C63 1.14 mm to (50.4, 67.9)
- moved Q5 1.14 mm to (46.8, 67.6)
- moved R57 1.14 mm to (43.6, 67.8)
- moved C29 1.14 mm to (41.9, 52.6)
- moved C36 1.14 mm to (64.2, 62.2)
- moved R11 1.14 mm to (62.8, 55.5)
- moved R17 1.14 mm to (50.5, 51.0)
- moved R55 1.14 mm to (49.8, 60.1)
- moved R8 1.14 mm to (64.4, 52.6)
- moved C30 1.14 mm to (62.6, 50.7)
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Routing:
- net /inverter/1GH_A: track 13.6 -> 11.4 mm
- net +3V3: track 44.5 -> 42.6 mm

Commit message: motorDriver pcb update
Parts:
- moved J4 17.6 mm to (110.8, 34.1)
- moved C29 4.96 mm to (40.7, 57.4), turned to 180 degrees
- moved R47 4.51 mm to (97.0, 58.6)
- moved R43 4.50 mm to (98.9, 58.6)
- moved R44 4.39 mm to (93.8, 58.6), turned to -90 degrees
- moved J5 3.30 mm to (41.5, 38.8)
- moved C33 2.87 mm to (40.7, 59.5), turned to 180 degrees
- moved C60 2.30 mm to (84.9, 64.7), turned to 90 degrees
- moved C59 2.24 mm to (86.5, 65.6), turned to 90 degrees
- moved J1 2.05 mm to (35.3, 51.0)
- moved R36 0.87 mm to (79.6, 69.2)
- moved C52 0.87 mm to (75.0, 69.2)
- moved C53 0.87 mm to (76.5, 69.1)
- moved C54 0.87 mm to (81.2, 69.2)
- moved C55 0.87 mm to (82.7, 69.2)
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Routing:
- net /OP_VCC: track 0.00 -> 65.2 mm
- net /1B_ISENSOR_N: track 2.23 -> 25.8 mm, vias 0 -> 1
- net /1B_ISENSOR_P: track 2.41 -> 21.6 mm, vias 0 -> 1
- net /VREF_OP1: track 0.00 -> 18.7 mm
- net /VREF_OP2: track 0.00 -> 8.70 mm
- net Net-(U8A-+): track 0.00 -> 8.07 mm
- net Net-(R54-Pad2): track 0.00 -> 8.05 mm
- net Net-(R60-Pad2): track 0.00 -> 7.61 mm
- net Net-(U8B-+): track 0.00 -> 6.71 mm
- net /INA2+: track 0.00 -> 6.55 mm
- net Net-(Q1-G): track 1.60 -> 8.06 mm
- net /INA1+: track 0.00 -> 6.21 mm
- net Net-(U8A--): track 0.00 -> 5.63 mm
- net /inverter/2GH_A: track 14.8 -> 9.84 mm
- net Net-(Q11-G): track 16.6 -> 12.0 mm
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- added copper zone on F.Cu, net /VREF_OP1
- added copper zone on In1.Cu, net GNDD

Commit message: update motorDriver pcb
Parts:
- removed C47: 10n, Capacitor_SMD:C_0603_1608Metric_Pad1.08x0.95mm_HandSolder
- removed C48, C50: 100n, Capacitor_SMD:C_0603_1608Metric_Pad1.08x0.95mm_HandSolder
- removed C49: 2.2U, Capacitor_SMD:C_0603_1608Metric_Pad1.08x0.95mm_HandSolder
- removed R74: 4.7k, Resistor_SMD:R_0603_1608Metric_Pad0.98x0.95mm_HandSolder
- removed U5: MPU6500, balancerDriver:QFN-24_L3.0-W3.0-P0.40-BL-EP
- added C13: 10n, Capacitor_SMD:C_0603_1608Metric_Pad1.08x0.95mm_HandSolder, F.Cu at (75.5, 61.7)
- added C22: 100n, Capacitor_SMD:C_0603_1608Metric_Pad1.08x0.95mm_HandSolder, F.Cu at (79.0, 61.8)
- added C23: 100n, Capacitor_SMD:C_0603_1608Metric_Pad1.08x0.95mm_HandSolder, F.Cu at (75.4, 59.2)
- added C24: 2.2n, Capacitor_SMD:C_0603_1608Metric_Pad1.08x0.95mm_HandSolder, F.Cu at (82.9, 59.4)
- added FB1: FerriteBead, Capacitor_SMD:C_0603_1608Metric_Pad1.08x0.95mm_HandSolder, F.Cu at (75.4, 55.8)
- added U4: MPU-6050, Sensor_Motion:InvenSense_QFN-24_4x4mm_P0.5mm, F.Cu at (79.0, 58.1)
- J2: footprint Connector_PinSocket_2.54mm:PinSocket_1x06_P2.54mm_Vertical -> Connector_PinHeader_2.54mm:PinHeader_1x06_P2.54mm_Vertical
- J3, J5: footprint balancerDriver:CONN-SMD_BM06B-GHS-TBT-LF-SN -> balancerDriver:CONN-SMD_6P-P1.00_MEGASTAR_ZX-SH1.0-6PWT
- R49: value 10K -> 10k
- moved J4 12.8 mm to (98.0, 34.4)
- moved J2 10.2 mm to (78.8, 32.8), turned to 90 degrees
- moved J3 7.61 mm to (110.2, 43.5)
- moved J5 7.59 mm to (41.3, 46.4)
- moved J1 5.05 mm to (35.6, 56.0)
- moved C58 2.31 mm to (83.8, 61.9), turned to 180 degrees
- moved R72 2.30 mm to (80.0, 54.4)
- moved R73 1.63 mm to (82.9, 56.0), turned to -90 degrees
- moved R49 1.60 mm to (73.6, 58.2), turned to -90 degrees
- moved C52 1.07 mm to (75.0, 70.2)
- moved C59 1.07 mm to (86.5, 66.7)
- moved R36 1.07 mm to (79.6, 70.3)
- moved U6 1.07 mm to (80.0, 65.4)
- moved C53 1.07 mm to (76.5, 70.2)
- moved C54 1.07 mm to (81.2, 70.3)
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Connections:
- net /1A_ISENSOR_N renamed /1A_ISENSOR-
- net /1B_ISENSOR_N renamed /1B_ISENSOR-
- net /1B_ISENSOR_P renamed /1B_ISENSOR+
- net /2A_ISENSOR_N renamed /2A_ISENSOR-
- net /2A_ISENSOR_P renamed /2A_ISENSOR+
- net /2B_ISENSOR_N renamed /2B_ISENSOR-
- net /2B_ISENSOR_P renamed /2B_ISENSOR+
- C30 pad 2: Net-(C30-Pad2) -> /1A_ISENSOR+
- C62 pad 2: /M1_ADC1_INx -> /M1_ADC1_IN4
- C63 pad 2: /M1_ADC1_INx -> /M1_ADC2_IN7
- C64 pad 2: /M2_ADC1_INx -> /M2_ADC2_IN14
- C65 pad 2: /M2_ADC1_INx -> /M2_ADC1_IN11
- J3 pad 1: /SPI1_SCK -> GNDD
- J3 pad 2: /SPI1_MISO -> +3V3
- J3 pad 3: /SPI1_MOSI -> /NSS2
- J3 pad 4: unconnected-(J3-Pin_4-Pad4) -> /SPI1_SCK
- J3 pad 5: +3V3 -> /SPI1_MISO
- J3 pad 6: GNDD -> /SPI1_MOSI
- J4 pad 1: /STM_RX -> GNDD
- J4 pad 2: /STM_TX -> /USART1_RX
- J4 pad 3: GNDD -> /USART1_TX
- J5 pad 1: /SPI1_SCK -> GNDD
- J5 pad 2: /SPI1_MISO -> +3V3
- J5 pad 3: /SPI1_MOSI -> /NSS1
- J5 pad 4: unconnected-(J5-Pin_4-Pad4) -> /SPI1_SCK
- J5 pad 5: +3V3 -> /SPI1_MISO
- J5 pad 6: GNDD -> /SPI1_MOSI
- R49 pad 1: +3V3 -> Net-(U4-VDD)
- R55 pad 2: /M1_ADC1_INx -> /M1_ADC1_IN4
- R56 pad 2: /1A_ISENSOR_P -> /1A_ISENSOR+
- R61 pad 2: /M1_ADC1_INx -> /M1_ADC2_IN7
- R66 pad 2: /M2_ADC1_INx -> /M2_ADC2_IN14
- R7 pad 2: Net-(C30-Pad2) -> /1A_ISENSOR+
- R71 pad 2: /M2_ADC1_INx -> /M2_ADC1_IN11
- R72 pad 1: /SDA -> Net-(U4-VDD)
- R72 pad 2: +3V3 -> /I2C2_SDA
- R73 pad 1: /SCL -> Net-(U4-VDD)
- R73 pad 2: +3V3 -> /I2C2_SCL
- U2 pad 14: /STM32_TX -> unconnected-(U2-PA2-Pad14)
- U2 pad 17: /STM32_RX -> /M1_ADC1_IN4
- U2 pad 18: unconnected-(U2-PA4-Pad18) -> /M1_ADC2_IN7
- U2 pad 19: /SPI1_SCK -> unconnected-(U2-PA5-Pad19)
- U2 pad 20: /SPI1_MISO -> unconnected-(U2-PA6-Pad20)
- U2 pad 22: unconnected-(U2-PC4-Pad22) -> /I2C2_SCL
- U2 pad 30: /USART3_TX -> unconnected-(U2-PB10-Pad30)
- U2 pad 33: /USART3_RX -> /M2_ADC2_IN14
- U2 pad 34: unconnected-(U2-PB12-Pad34) -> /M2_ADC1_IN11
- U2 pad 42: unconnected-(U2-PA8-Pad42) -> /I2C2_SDA
- U2 pad 43: unconnected-(U2-PA9-Pad43) -> /USART1_TX
- U2 pad 44: unconnected-(U2-PA10-Pad44) -> /USART1_RX
- U2 pad 45: unconnected-(U2-PA11-Pad45) -> /NSS2
- U2 pad 52: unconnected-(U2-PC10-Pad52) -> /TIM8_CH1N
- U2 pad 55: unconnected-(U2-PD2-Pad55) -> /NSS1
- U2 pad 56: /TIM8_CH1N -> /SPI1_SCK
- U2 pad 57: unconnected-(U2-PB4-Pad57) -> /SPI1_MISO
- U2 pad 61: unconnected-(U2-PB8-Pad61) -> /USART3_RX
- U2 pad 62: unconnected-(U2-PB9-Pad62) -> /USART3_TX
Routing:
- net /SPI1_MISO: track 0.00 -> 88.7 mm, vias 0 -> 2
- net /SPI1_SCK: track 0.00 -> 72.8 mm, vias 0 -> 2
- net /SPI1_MOSI: track 0.00 -> 72.6 mm, vias 0 -> 2
- net /NSS1: track 0.00 -> 45.3 mm
- net /M1_ADC2_IN7: track 0.00 -> 39.5 mm
- net /M2_ADC1_IN11: track 0.00 -> 35.4 mm
- net /M1_ADC1_IN4: track 0.00 -> 32.8 mm
- net /M2_ADC2_IN14: track 0.00 -> 27.3 mm
- net /2B_ISENSOR+: track 1.81 -> 28.5 mm, vias 0 -> 1
- net /2B_ISENSOR-: track 1.94 -> 27.2 mm, vias 0 -> 1
- net /NSS2: track 0.00 -> 20.5 mm, vias 0 -> 2
- net /1A_ISENSOR-: track 1.90 -> 21.6 mm, vias 0 -> 1
- net /1A_ISENSOR+: track 0.00 -> 17.9 mm, vias 0 -> 1
- net /USART1_RX: track 0.00 -> 16.2 mm, vias 0 -> 2
- net /2A_ISENSOR-: track 1.65 -> 17.7 mm, vias 0 -> 1
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
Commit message: update driver pcn
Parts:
- C29, C31, C33, C34, C35, C37, C39, C40, C41, C43, C45, C46: footprint Capacitor_SMD:C_0805_2012Metric_Pad1.18x1.45mm_HandSolder -> Capacitor_SMD:C_1206_3216Metric_Pad1.33x1.80mm_HandSolder
- moved C29 0.53 mm to (40.3, 57.0)
- moved C33 0.53 mm to (40.3, 59.1)
- moved C35 0.53 mm to (40.2, 65.6)
- moved C39 0.53 mm to (40.2, 67.8)
- moved C41 0.53 mm to (40.2, 61.3)
- moved C45 0.53 mm to (40.2, 63.5)
- moved R18 0.42 mm to (64.1, 58.8)
- moved C31 0.26 mm to (117.3, 52.7)
- moved C43 0.26 mm to (117.2, 58.3)
- moved C34 0.26 mm to (117.3, 55.2)
- moved C37 0.26 mm to (117.3, 65.7)
- moved C40 0.26 mm to (117.3, 63.6)
- moved C46 0.26 mm to (117.2, 60.6)
- moved J1 0.26 mm to (35.5, 55.8)
- moved C13 0.22 mm to (75.5, 61.9)
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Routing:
- net GNDPWR: track 9.57 -> 208.5 mm, vias 0 -> 88
- net GNDD: track 3.32 -> 114.3 mm, vias 7 -> 41
- net +12V: track 0.00 -> 78.2 mm, vias 0 -> 5
- net /OP_VCC: track 49.7 -> 95.7 mm, vias 0 -> 6
- net /VREF_OP1: track 18.7 -> 52.5 mm, vias 0 -> 2
- net /inverter/1SH_W: track 21.7 -> 51.9 mm, vias 9 -> 11
- net /VREF_OP2: track 16.8 -> 46.5 mm
- net Net-(U4-VDD): track 12.7 -> 24.7 mm, vias 0 -> 4
- net +3V3: track 35.8 -> 40.3 mm, vias 1 -> 3
- net Net-(Q12-G): track 3.54 -> 7.70 mm
- net /TIM8_CH1N: track 12.9 -> 14.1 mm
- net /TIM8_CH2N: track 13.3 -> 14.0 mm
- net /MPU_INT: track 3.55 -> 4.14 mm, vias 0 -> 2
- net /SPI1_MISO: track 88.7 -> 89.3 mm
- added copper zone on B.Cu, net GNDPWR
